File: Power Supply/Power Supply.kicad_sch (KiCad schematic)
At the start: 25 parts, among them U1 LM1085-12, U2 LM7912_TO220

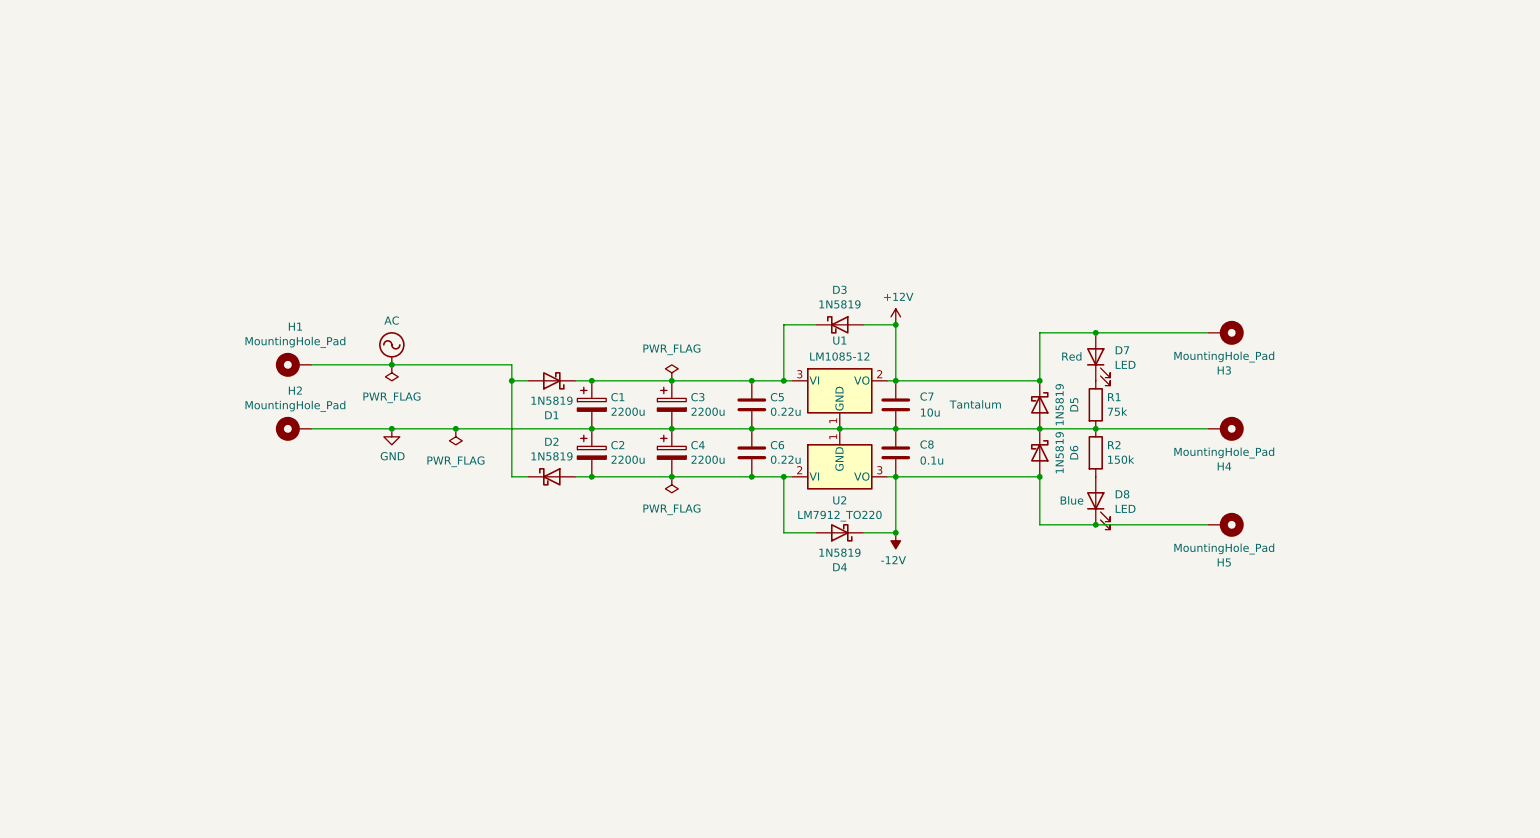
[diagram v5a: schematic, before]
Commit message: Place PSU components on PCB
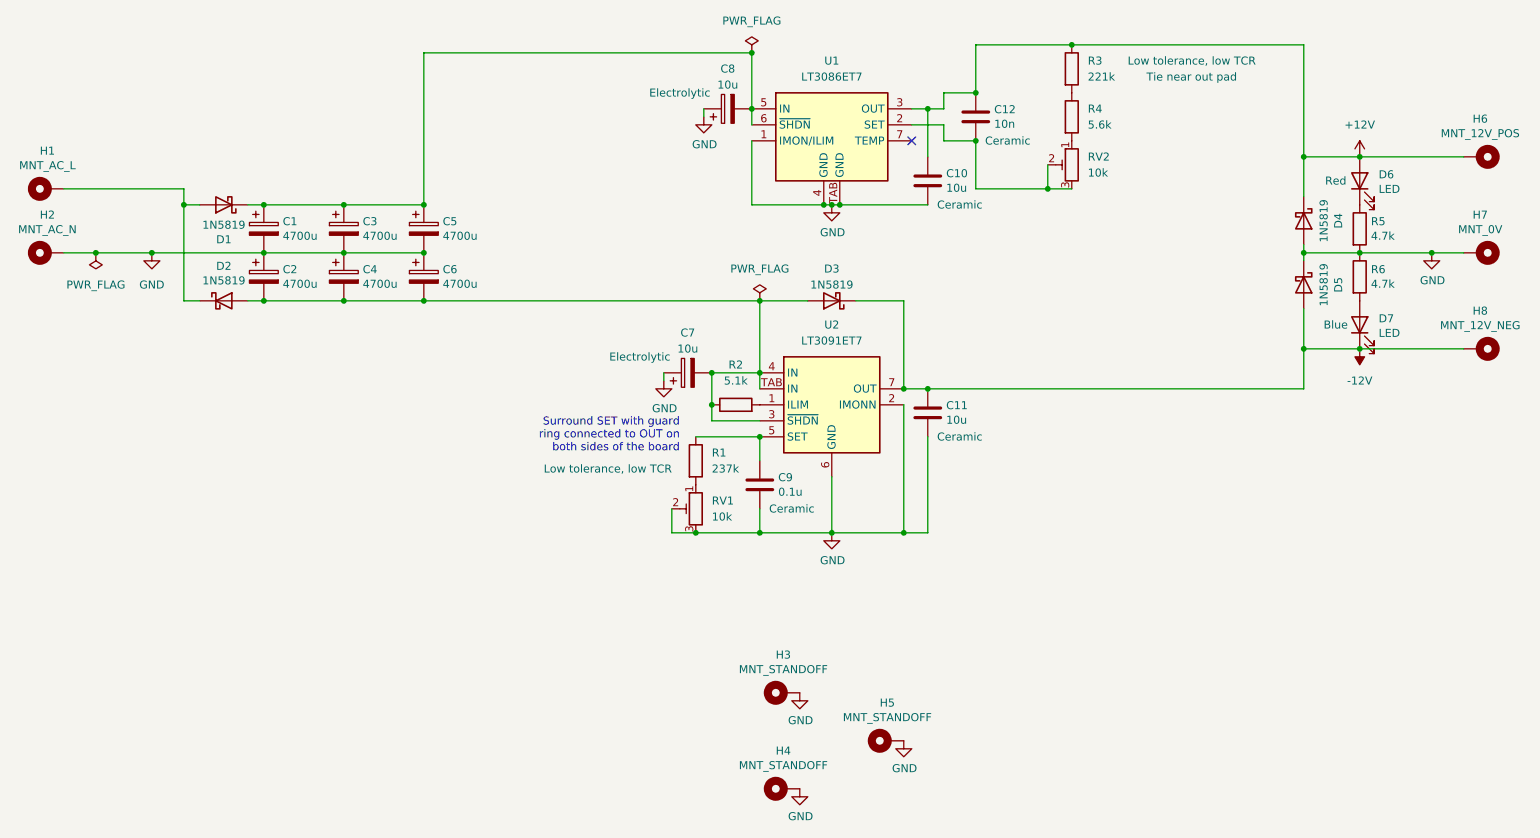
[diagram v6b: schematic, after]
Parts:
- removed C5, C6: 0.22u, Capacitor_THT:C_Disc_D5.0mm_W2.5mm_P5.00mm, symbol Device:C
- removed C7: 10u, Capacitor_THT:C_Disc_D5.0mm_W2.5mm_P5.00mm, symbol Device:C
- removed C8: 0.1u, Capacitor_THT:C_Disc_D5.0mm_W2.5mm_P5.00mm, symbol Device:C
- removed D4: 1N5819, Diode_THT:D_DO-41_SOD81_P3.81mm_Vertical_KathodeUp, symbol Diode:1N5819
- removed U1: LM1085-12, symbol Regulator_Linear:LM1085-12
- removed U2: LM7912_TO220, Package_TO_SOT_THT:TO-220-3_Vertical, symbol Regulator_Linear:LM7912_TO220
- added C10, C11: 10u, 0_Capacitor_THT:C_Disc_D5.5mm_W4.0mm_P2.50mm, symbol Device:C
- added C12: 10n, 0_Capacitor_THT:C_Disc_D5.5mm_W2.5mm_P2.50mm, symbol Device:C
- added C3, C4: 4700u, Capacitor_THT:CP_Radial_D18.0mm_P7.50mm, symbol Device:C_Polarized
- added C7, C8: 10u, Capacitor_THT:CP_Radial_D5.0mm_P2.50mm, symbol Device:C_Polarized
- added C9: 0.1u, 0_Capacitor_THT:C_Disc_D5.5mm_W2.5mm_P2.50mm, symbol Device:C
- added H3, H4, H5: MNT_STANDOFF, 0_MountingHole:MountingHole_Pitch7.5mm_Drill3.4mm, symbol Mechanical:MountingHole_Pad
- added R1: 237k, Resistor_THT:R_Axial_DIN0207_L6.3mm_D2.5mm_P7.62mm_Horizontal, symbol Device:R
- added R2: 5.1k, Resistor_THT:R_Axial_DIN0207_L6.3mm_D2.5mm_P7.62mm_Horizontal, symbol Device:R
- added R3: 221k, Resistor_THT:R_Axial_DIN0207_L6.3mm_D2.5mm_P7.62mm_Horizontal, symbol Device:R
- added R4: 5.6k, Resistor_THT:R_Axial_DIN0207_L6.3mm_D2.5mm_P7.62mm_Horizontal, symbol Device:R
- added RV1, RV2: 10k, Potentiometer_THT:Potentiometer_Bourns_3296W_Vertical, symbol Device:R_Potentiometer_Trim
- added U1: LT3086ET7, 0_Package_TO_SOT_THT:TO-220-7_P2.54x3.7mm_StaggerOdd_Lead3.8mm_Vertical_HeatSink, symbol 0_Regulator_Linear:LT3086ET7
- added U2: LT3091ET7, 0_Package_TO_SOT_THT:TO-220-7_P2.54x3.7mm_StaggerOdd_Lead3.8mm_Vertical_HeatSink, symbol 0_Regulator_Linear:LT3091ET7
- C1, C2: value 2200u -> 4700u; footprint Capacitor_THT:CP_Radial_D16.0mm_P7.50mm -> Capacitor_THT:CP_Radial_D18.0mm_P7.50mm
- C5: renamed from C3; value 2200u -> 4700u; footprint Capacitor_THT:CP_Radial_D16.0mm_P7.50mm -> Capacitor_THT:CP_Radial_D18.0mm_P7.50mm
- C6: renamed from C4; value 2200u -> 4700u; footprint Capacitor_THT:CP_Radial_D16.0mm_P7.50mm -> Capacitor_THT:CP_Radial_D18.0mm_P7.50mm
- D1, D2, D3: footprint Diode_THT:D_DO-41_SOD81_P3.81mm_Vertical_KathodeUp -> Diode_THT:D_DO-41_SOD81_P10.16mm_Horizontal
- D4: renamed from D5; footprint Diode_THT:D_DO-41_SOD81_P3.81mm_Vertical_KathodeUp -> Diode_THT:D_DO-41_SOD81_P10.16mm_Horizontal
- D5: renamed from D6; footprint Diode_THT:D_DO-41_SOD81_P3.81mm_Vertical_KathodeUp -> Diode_THT:D_DO-41_SOD81_P10.16mm_Horizontal
- H1: value MountingHole_Pad -> MNT_AC_L; footprint Connector_PinSocket_2.54mm:PinSocket_1x01_P2.54mm_Vertical -> 0_MountingHole:MountingHole_Pitch1.7mm_Drill1mm
- H2: value MountingHole_Pad -> MNT_AC_N; footprint Connector_PinSocket_2.54mm:PinSocket_1x01_P2.54mm_Vertical -> 0_MountingHole:MountingHole_Pitch1.7mm_Drill1mm
- H6: renamed from H3; value MountingHole_Pad -> MNT_12V_POS; footprint Connector_PinSocket_2.54mm:PinSocket_1x01_P2.54mm_Vertical -> 0_MountingHole:MountingHole_Pitch12mm_Drill6.4mm
- H7: renamed from H4; value MountingHole_Pad -> MNT_0V; footprint Connector_PinSocket_2.54mm:PinSocket_1x01_P2.54mm_Vertical -> 0_MountingHole:MountingHole_Pitch12mm_Drill6.4mm
- H8: renamed from H5; value MountingHole_Pad -> MNT_12V_NEG; footprint Connector_PinSocket_2.54mm:PinSocket_1x01_P2.54mm_Vertical -> 0_MountingHole:MountingHole_Pitch12mm_Drill6.4mm
- R5: renamed from R1; value 75k -> 4.7k
- R6: renamed from R2; value 150k -> 4.7k
- renumbered D7 to D6, D8 to D7
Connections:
- net +12V: now also C10.1, C12.1, R3.1, U1.3 (OUT); no longer D3.2 (A)
- net -12V: now also D3.1 (K), C11.1, U2.7 (OUT)
- net GND: now also C10.2, C11.2, C3.2, C4.1, C7.1, C8.1, C9.2, H3.1, H4.1, H5.1, RV1.2, RV1.3, U1.1 (IMON/ILIM), U1.4 (GND), U1.TAB (GND), U2.2 (IMONN), U2.6 (GND)
- net at C2.2, C6.2, D2.2 (A): now also D3.2 (A), C4.2, C7.2, R2.1, U2.3 (~{SHDN}), U2.4 (IN), U2.TAB (IN)
- net at C1.1, C5.1, D1.1 (K): now also C3.1, C8.2, U1.5 (IN), U1.6 (~{SHDN}); no longer D3.1 (K)
- net AC: no longer names the net of D1.2 (A), D2.1 (K), H1.1
- new net: R4.2, RV2.1
- new net: C12.2, RV2.2, RV2.3, U1.2 (SET)
- new net: R2.2, U2.1 (ILIM)
- new net: R3.2, R4.1
- new net: C9.1, R1.1, U2.5 (SET)
- new net: R1.2, RV1.1
- no-connect marks 0 -> 1
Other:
- note added: "Surround SET with guard ring connected to OUT on both sides of the board"
- moved on the sheet: C1, C2, C5, C6, D1, D2, D4, D5, D6, D7, H1, H2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

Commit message: Create additional filled zones
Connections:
- net AC_REC_P: now reaches C1.1, C3.1, C5.1, C8.2, D1.1 (K), U1.5 (IN), U1.6 (~{SHDN})
- net AC_REC_N: now reaches C2.2, C4.2, C6.2, C7.2, D2.2 (A), D3.2 (A), R2.1, U2.3 (~{SHDN}), U2.4 (IN), U2.TAB (IN)
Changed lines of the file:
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@@
+    (stroke (width 0) (type default))
+  )
+  (wire (pts (xy 77.47 81.28) (xy 77.47 82.55))
     (stroke (width 0) (type default))
   )
@@
   )
   (wire (pts (xy 33.02 63.5) (xy 52.07 63.5))
+    (stroke (width 0) (type default))
+  )
+  (wire (pts (xy 77.47 64.77) (xy 77.47 66.04))
     (stroke (width 0) (type default))
   )
@@
     (effects (font (size 1.27 1.27)) (justify right bottom))
   )
+  (global_label "AC_REC_N" (shape output) (at 77.47 82.55 270) (fields_autoplaced)
+    (effects (font (size 1.27 1.27)) (justify right))
+    (property "Intersheetrefs" "${INTERSHEET_REFS}" (at 77.47 94.1943 90)
+      (effects (font (size 1.27 1.27)) (justify right) hide)
+    )
+  )
+  (global_label "AC_REC_P" (shape output) (at 77.47 64.77 90) (fields_autoplaced)
+    (effects (font (size 1.27 1.27)) (justify left))
+    (property "Intersheetrefs" "${INTERSHEET_REFS}" (at 77.47 53.1862 90)
+      (effects (font (size 1.27 1.27)) (justify left) hide)
+    )
+  )
   (symbol (lib_id "Device:C_Polarized") (at 64.77 69.85 0) (unit 1)
